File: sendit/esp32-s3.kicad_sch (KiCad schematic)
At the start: 47 parts, among them J9 USB_TYPE_C_16PIN, Q1 FDC6330L, Q2 S8050, Q3 S8050, SW1 RESET, SW2 BOOT, U1 ESP32-S3-WROOM-1-N16R8, U2 USBLC6-2SC6, U3 XC6210B332MR, U4 SN74LV1T34DBV, U5 CH334F, U6 CH343P, Y1 12Mhz

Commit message: big change removing the usb hub and serial chip.
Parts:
- removed C11, C6: 15pF, Capacitor_SMD:C_0603_1608Metric, symbol Device:C_Small
- removed C14, C15, C17: 100nF, Capacitor_SMD:C_0603_1608Metric, symbol Device:C_Small
- removed C16: 10uF, Capacitor_SMD:C_0603_1608Metric, symbol Device:C_Small
- removed C8, C9: 1uF, Capacitor_SMD:C_0603_1608Metric, symbol Device:C_Small
- removed Q1: FDC6330L, Package_TO_SOT_SMD:TSOT-23-6, symbol Transistor_FET:FDC6330L
- removed Q2, Q3: S8050, Package_TO_SOT_SMD:SOT-23, symbol Transistor_BJT:Q_NPN_BEC
- removed R10: 100R, Resistor_SMD:R_0603_1608Metric, symbol Device:R_Small_US
- removed R11, R12: 100k, Resistor_SMD:R_0603_1608Metric, symbol Device:R_Small_US
- removed R15: 1k, Resistor_SMD:R_0603_1608Metric, symbol Device:R_Small_US
- removed R17, R18: 10k, Resistor_SMD:R_0603_1608Metric, symbol Device:R_Small_US
- removed U5: CH334F, yarrboard:QFN-24-1EP_4x4mm_P0.5mm_EP2.7x2.7mm_ThermalVias, symbol yarrboard:CH334F
- removed U6: CH343P, yarrboard:QFN-16-1EP_3x3mm_P0.5mm_EP1.7x1.7mm_ThermalVias, symbol Interface_USB:CH343P
- removed Y1: 12Mhz, Crystal:Crystal_SMD_SeikoEpson_TSX3225-4Pin_3.2x2.5mm, symbol Device:Crystal_GND24_Small
- added TP5, TP6: ~, TestPoint:TestPoint_THTPad_D1.5mm_Drill0.7mm, symbol Connector:TestPoint
- renumbered C13 to C10, C12 to C11, C7 to C4, C4 to C5, C5 to C6, C18 to C7, C19 to C8, C10 to C9, J9 to J10, R13 to R10, R14 to R11, R19 to R12, R20 to R13, R16 to R14, TP5 to TP7, U4 to U3, U3 to U4
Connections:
- net HUB_D+ is gone; now on net ESP_USB+: U2.1 (I/O1)
- net HUB_D- is gone; now on net ESP_USB-: U2.3 (I/O2)
- net EN: now also TP5.1
- net GPIO0_BOOT: now also TP6.1
- no-connect marks 19 -> 2
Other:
- note removed: "USB CHIPS POWER SAVER"
- note removed: "USB HUB"
- note removed: "USB TO SERIAL"
- moved on the sheet: C10, C11, C4, C5, C6, C7, C8, C9, D4, D5, R12, R13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

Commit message: first pass fully routed.
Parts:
- removed D5: GREEN, LED_SMD:LED_0603_1608Metric, symbol Device:LED
- removed R14: 5.1k, Resistor_SMD:R_0603_1608Metric, symbol Device:R_Small_US
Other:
- note removed: "POWER LED"

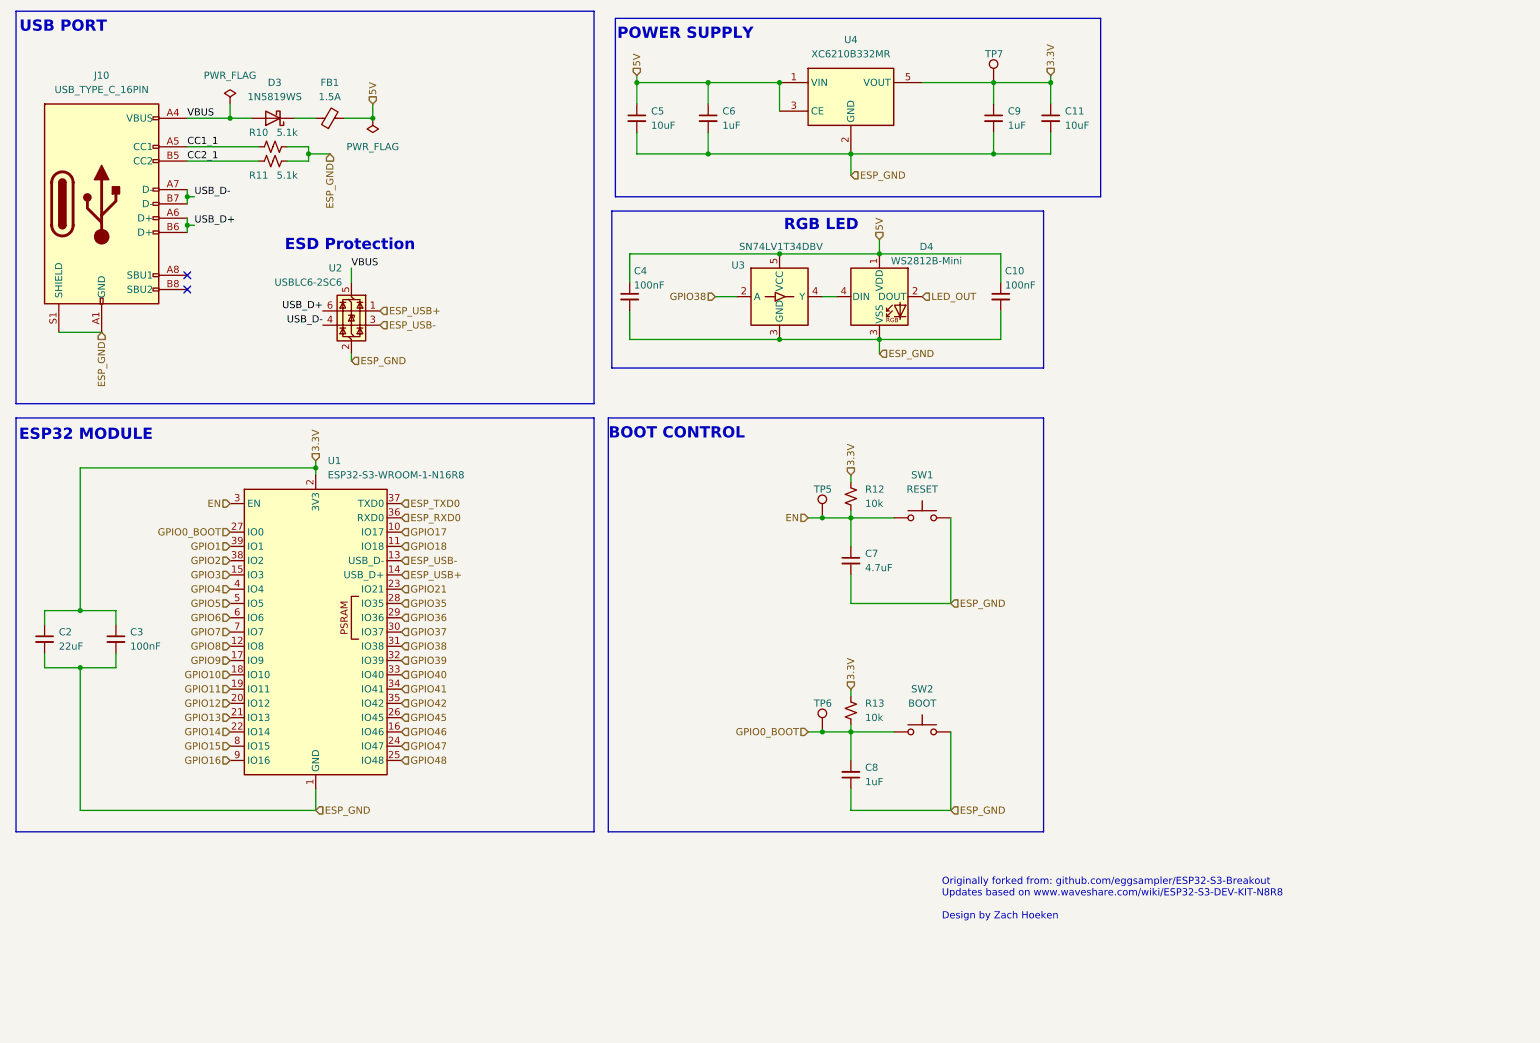
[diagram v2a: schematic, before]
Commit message: via stitching and calculations
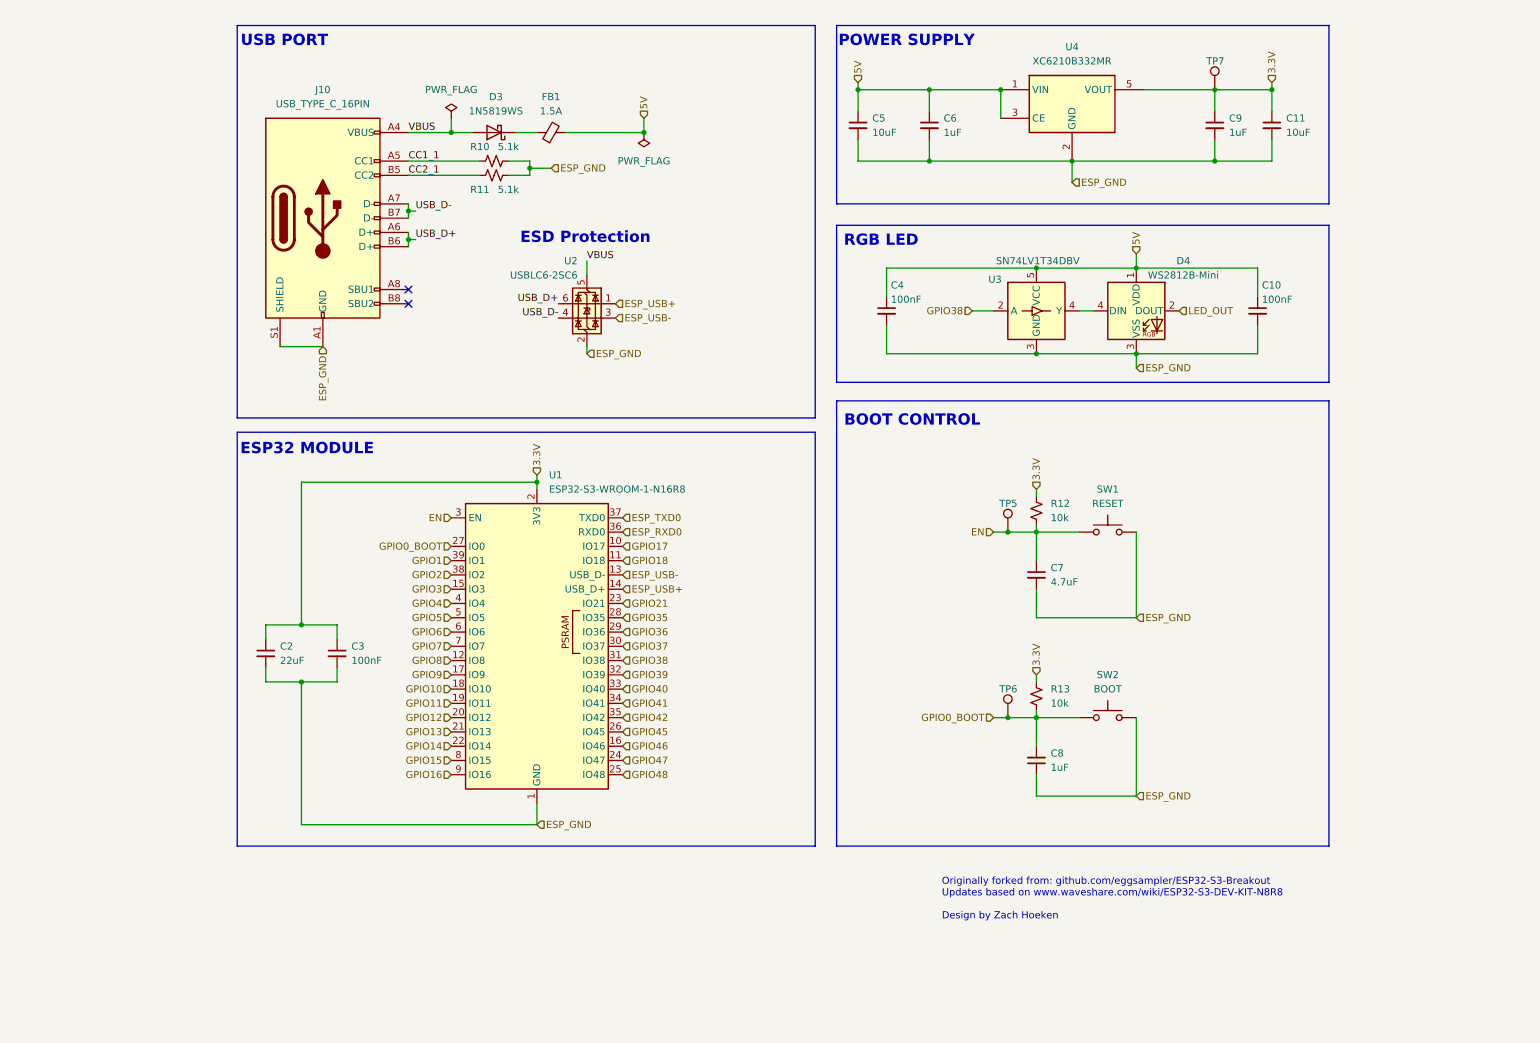
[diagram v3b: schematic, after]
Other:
- moved on the sheet: C10, C11, C2, C3, C4, C5, C6, C7, C8, C9, D3, D4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

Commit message: double checked power supplies + gave esp32-s3 proper voltage/ground symbols
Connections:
- net 3.3V renamed +3.3V
- net 5V renamed +5V
- net ESP_GND renamed GND

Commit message: moved the dc buck circuit away from the usb port.
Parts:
- SW1, SW2: Rotation Offset (none) -> 90
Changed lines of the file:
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@@
+			)
+		)
+		(property "Rotation Offset" "90"
+			(at 208.28 106.68 0)
+			(effects
+				(font
+					(size 1.27 1.27)
+				)
+				(hide yes)
 			)
 		)
@@
 			(at 208.28 139.7 0)
 			(effects
+				(font
+					(size 1.27 1.27)
+				)
+				(hide yes)
+			)
+		)
+		(property "Rotation Offset" "90"
+			(at 208.28 139.7 0)
+			(effects

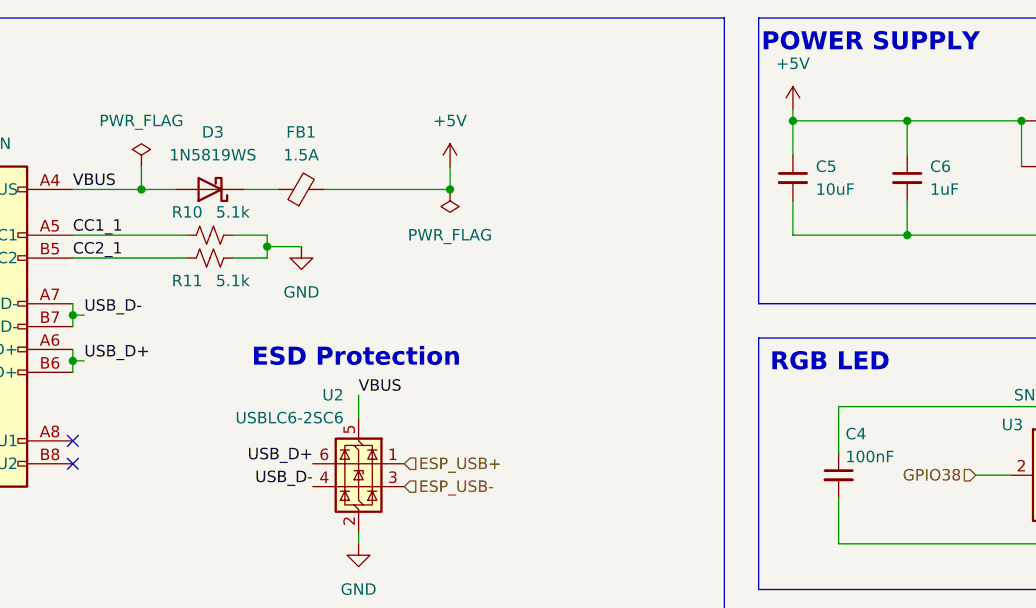
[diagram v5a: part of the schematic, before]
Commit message: added diode to prevent backfeed into 24v buck and beefed up 5v rail
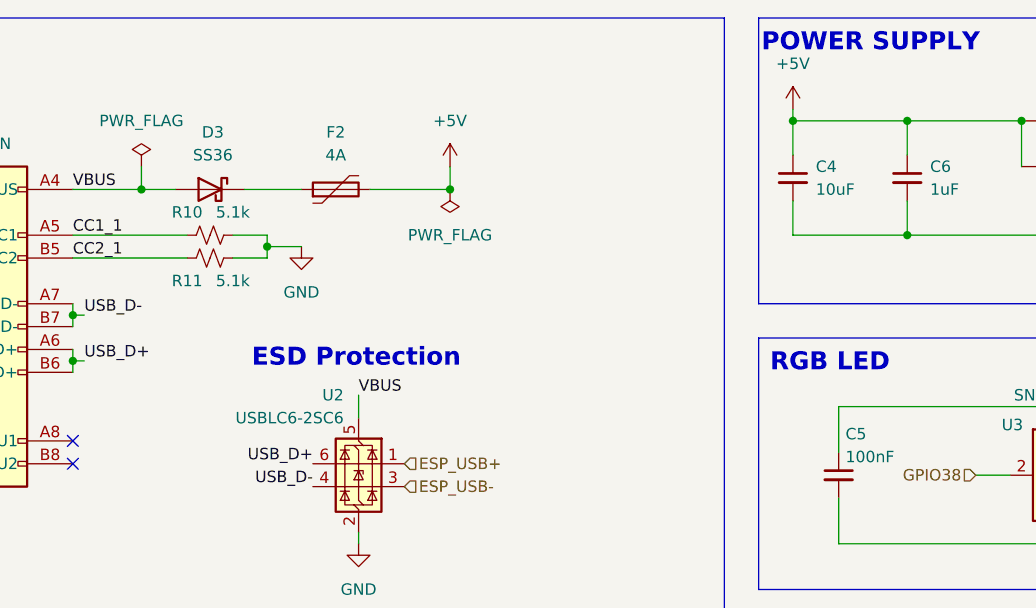
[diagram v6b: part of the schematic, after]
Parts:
- removed D3: 1N5819WS, Diode_SMD:D_SOD-323, symbol Diode:1N5819WS
- added D3: SS36, Diode_SMD:D_SMA, symbol Diode:SS36
- F2: renamed from FB1; value 1.5A -> 4A; symbol Device:FerriteBead_Small -> Device:Polyfuse; LCSC C2760275 -> C2760306
- renumbered C5 to C4, C4 to C5
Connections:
- net VBUS: now also D3.2 (A)
- net at F2.1: now also D3.1 (K)
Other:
- moved on the sheet: F2
